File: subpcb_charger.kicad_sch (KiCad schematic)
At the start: 27 parts, among them J10 Screw_Terminal_01x02, J17 Conn_01x02, J19 Conn_01x02, J3 Screw_Terminal_01x03, J56 Screw_Terminal_01x02, J57 Conn_01x02, J58 Screw_Terminal_01x02, J59 Conn_01x02, J60 Screw_Terminal_01x02, J61 Conn_01x02, J62 Screw_Terminal_01x02, J63 Conn_01x02, J66 67800-8005, J67 Conn_01x05, J9 Conn_01x02, U14 Fuse Holder, U15 Fuse Holder, U16 Fuse Holder, U17 Fuse Holder

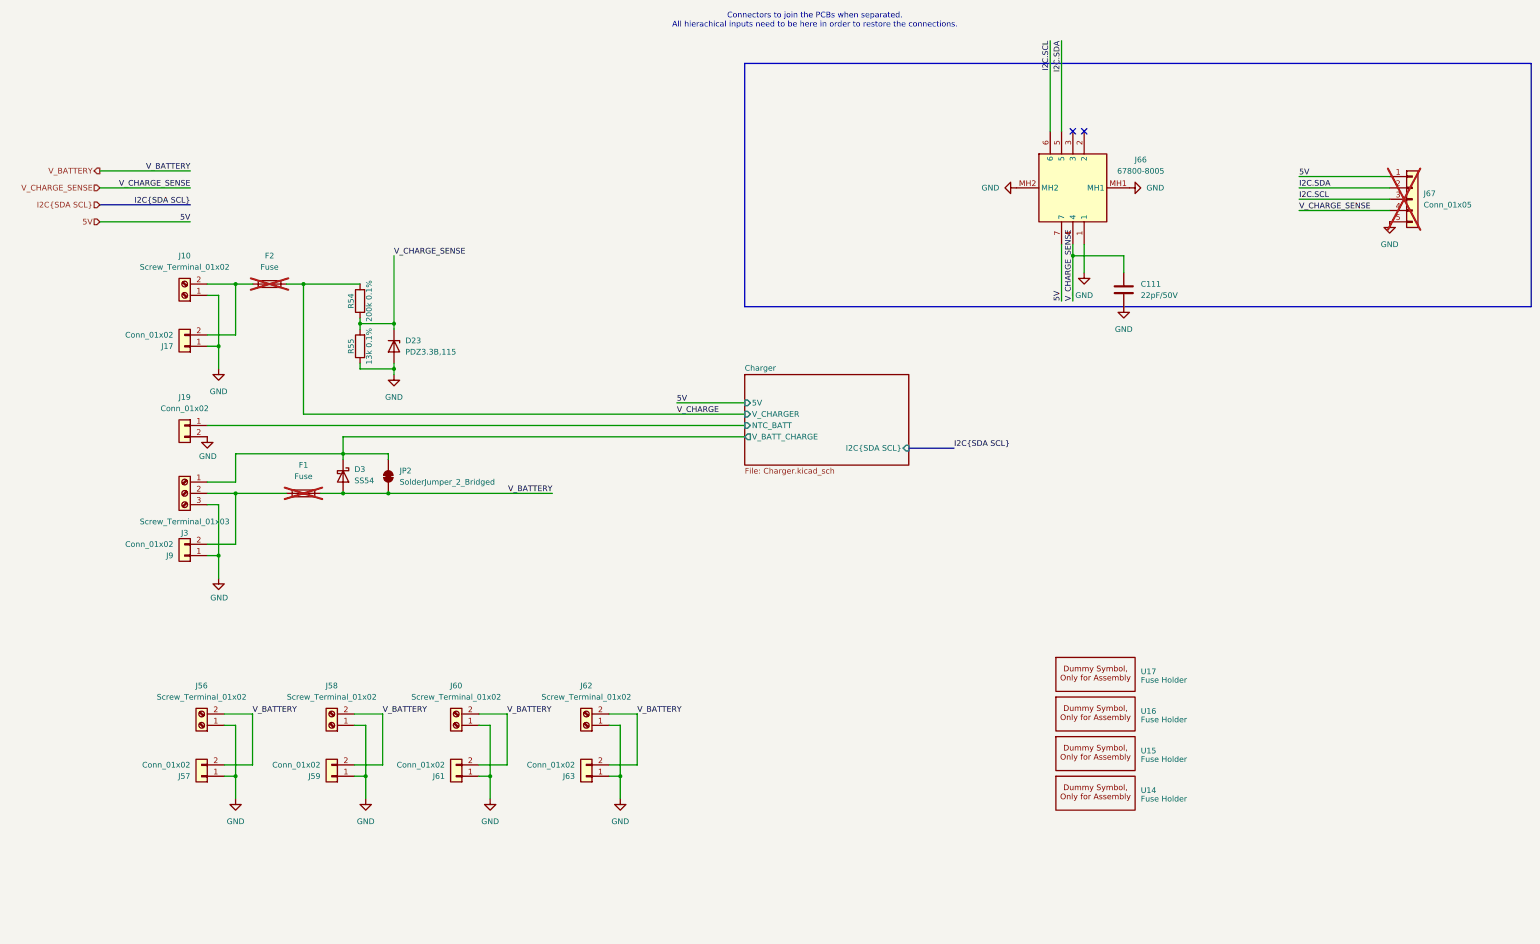
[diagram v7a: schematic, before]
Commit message: Switched SATA to XH connectors
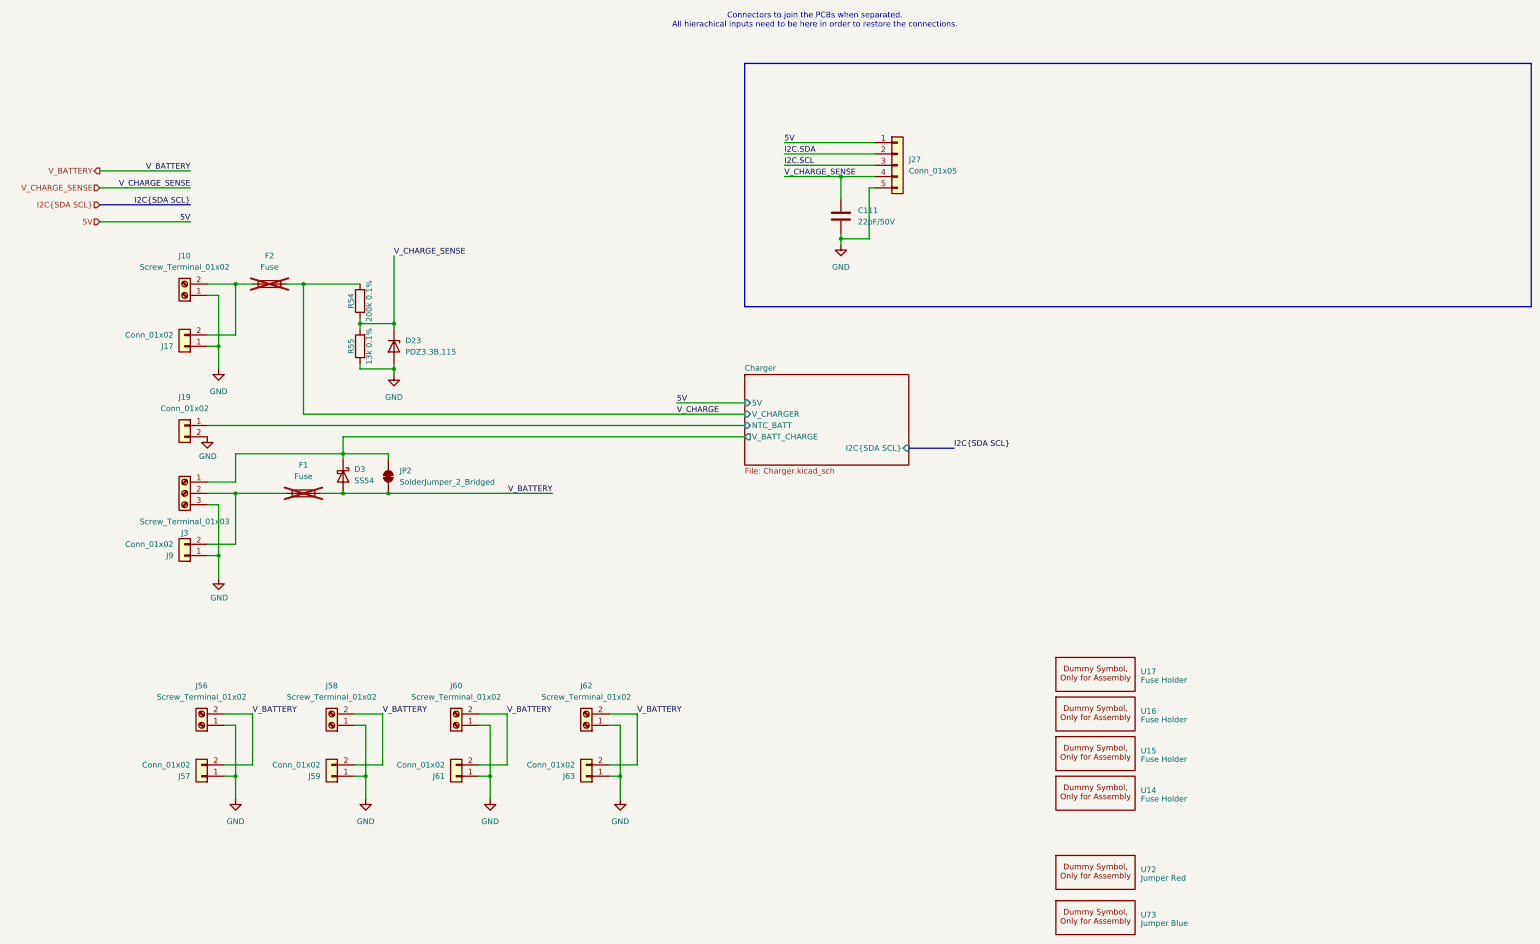
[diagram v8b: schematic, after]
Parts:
- removed J66: 67800-8005, SATA-Molex-67800-8005:SATA-Molex-67800-8005, symbol SATA-Molex-67800-8005:67800-8005
- removed J67: Conn_01x05, Connector_PinHeader_2.54mm:PinHeader_1x05_P2.54mm_Vertical, symbol Connector_Generic:Conn_01x05
- added J27: Conn_01x05, Connector_JST:JST_XH_B5B-XH-A_1x05_P2.50mm_Vertical, symbol Connector_Generic:Conn_01x05
- added U72: Jumper Red, xtech:Dummy, symbol xtech:Dummy
- added U73: Jumper Blue, xtech:Dummy, symbol xtech:Dummy
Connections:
- net 5V: now also J27.1 (Pin_1)
- net GND: now also J27.5 (Pin_5)
- net I2C.SCL: now also J27.3 (Pin_3)
- net I2C.SDA: now also J27.2 (Pin_2)
- net V_CHARGE_SENSE: now also J27.4 (Pin_4)
- no-connect marks 2 -> 0
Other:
- moved on the sheet: C111
